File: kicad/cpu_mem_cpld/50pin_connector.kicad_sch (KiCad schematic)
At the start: 1 part, among them P5 CONN_02X25

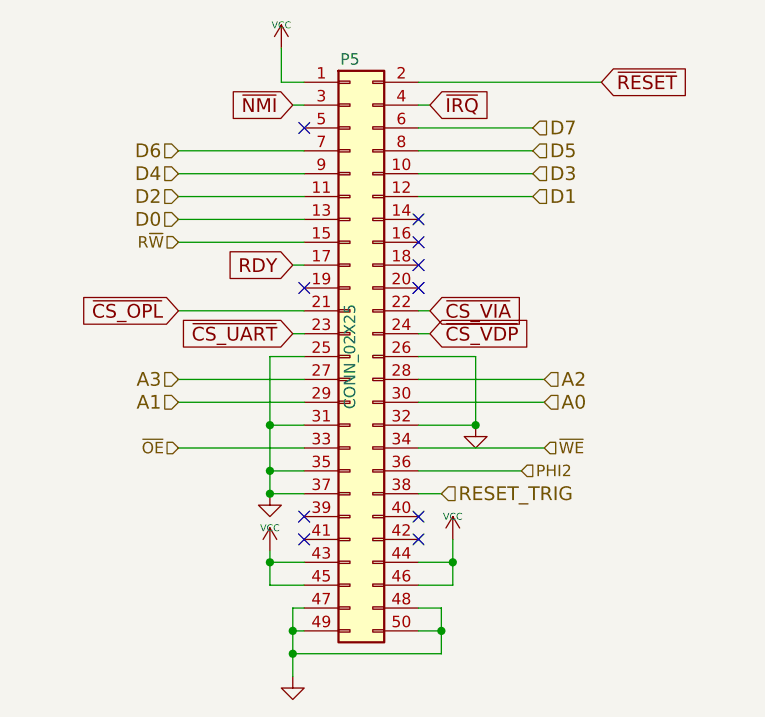
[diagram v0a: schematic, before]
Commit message: remove all global labels
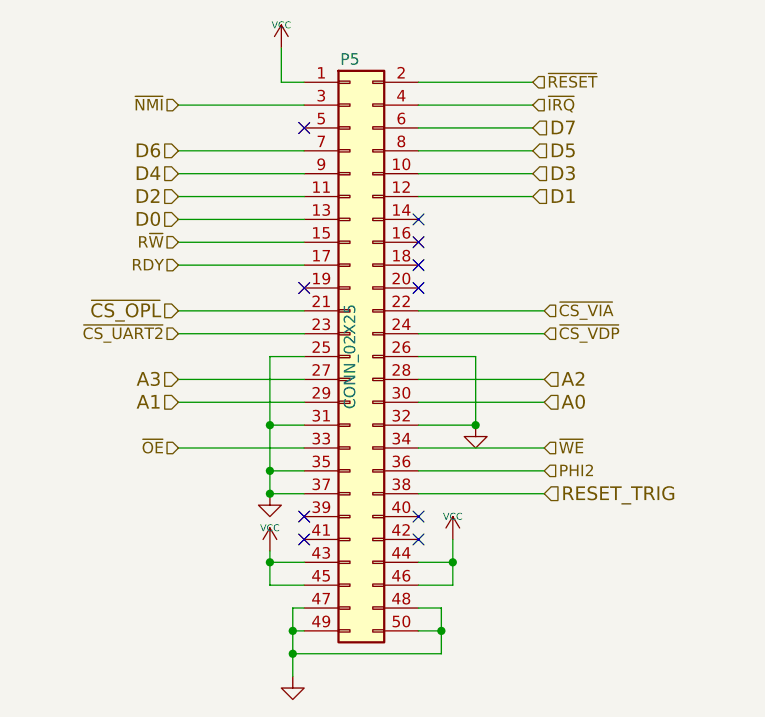
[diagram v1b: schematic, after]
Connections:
- net ~{CS_UART} renamed ~{CS_UART2}
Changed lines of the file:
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@@
     (stroke (width 0) (type default) (color 0 0 0 0))
   )
-  (wire (pts (xy 147.32 92.71) (xy 148.59 92.71))
+  (wire (pts (xy 147.32 92.71) (xy 161.29 92.71))
     (stroke (width 0) (type default) (color 0 0 0 0))
   )
@@
     (stroke (width 0) (type default) (color 0 0 0 0))
   )
-  (wire (pts (xy 147.32 64.77) (xy 167.64 64.77))
+  (wire (pts (xy 147.32 64.77) (xy 160.02 64.77))
     (stroke (width 0) (type default) (color 0 0 0 0))
   )
@@
     (stroke (width 0) (type default) (color 0 0 0 0))
   )
-  (wire (pts (xy 134.62 67.31) (xy 133.35 67.31))
+  (wire (pts (xy 134.62 67.31) (xy 120.65 67.31))
     (stroke (width 0) (type default) (color 0 0 0 0))
   )
@@
     (stroke (width 0) (type default) (color 0 0 0 0))
   )
-  (wire (pts (xy 147.32 90.17) (xy 148.59 90.17))
+  (wire (pts (xy 147.32 90.17) (xy 161.29 90.17))
     (stroke (width 0) (type default) (color 0 0 0 0))
   )
@@
     (stroke (width 0) (type default) (color 0 0 0 0))
   )
-  (wire (pts (xy 147.32 110.49) (xy 149.86 110.49))
+  (wire (pts (xy 147.32 110.49) (xy 161.29 110.49))
     (stroke (width 0) (type default) (color 0 0 0 0))
   )
@@
     (stroke (width 0) (type default) (color 0 0 0 0))
   )
-  (wire (pts (xy 147.32 67.31) (xy 148.59 67.31))
+  (wire (pts (xy 147.32 67.31) (xy 160.02 67.31))
     (stroke (width 0) (type default) (color 0 0 0 0))
   )
@@
     (stroke (width 0) (type default) (color 0 0 0 0))
   )
-  (wire (pts (xy 147.32 107.95) (xy 158.75 107.95))
+  (wire (pts (xy 147.32 107.95) (xy 161.29 107.95))
     (stroke (width 0) (type default) (color 0 0 0 0))
   )
@@
     (stroke (width 0) (type default) (color 0 0 0 0))
   )
-  (wire (pts (xy 133.35 85.09) (xy 134.62 85.09))
+  (wire (pts (xy 120.65 85.09) (xy 134.62 85.09))
     (stroke (width 0) (type default) (color 0 0 0 0))
   )
@@
     (stroke (width 0) (type default) (color 0 0 0 0))
   )
-  (wire (pts (xy 134.62 92.71) (xy 133.35 92.71))
+  (wire (pts (xy 120.65 92.71) (xy 134.62 92.71))
     (stroke (width 0) (type default) (color 0 0 0 0))
   )
@@
     (stroke (width 0) (type default) (color 0 0 0 0))
   )
-  (global_label "~{CS_VDP}" (shape input) (at 148.59 92.71 0) (fields_autoplaced)
-    (effects (font (size 1.524 1.524)) (justify left))
-    (property "Intersheet References" "${INTERSHEET_REFS}" (id 0) (at 0 0 0)
-      (effects (font (size 1.27 1.27)) hide)
-    )
-  )
-  (global_label "~{IRQ}" (shape input) (at 148.59 67.31 0) (fields_autoplaced)
-    (effects (font (size 1.524 1.524)) (justify left))
-    (property "Intersheet References" "${INTERSHEET_REFS}" (id 0) (at 0 0 0)
-      (effects (font (size 1.27 1.27)) hide)
-    )
-  )
-  (global_label "~{RESET}" (shape input) (at 167.64 64.77 0) (fields_autoplaced)
-    (effects (font (size 1.524 1.524)) (justify left))
-    (property "Intersheet References" "${INTERSHEET_REFS}" (id 0) (at 0 0 0)
-      (effects (font (size 1.27 1.27)) hide)
-    )
-  )
-  (global_label "~{NMI}" (shape input) (at 133.35 67.31 180) (fields_autoplaced)
-    (effects (font (size 1.524 1.524)) (justify right))
-    (property "Intersheet References" "${INTERSHEET_REFS}" (id 0) (at 0 0 0)
-      (effects (font (size 1.27 1.27)) hide)
-    )
-  )
-  (global_label "~{CS_UART}" (shape input) (at 133.35 92.71 180) (fields_autoplaced)
-    (effects (font (size 1.524 1.524)) (justify right))
-    (property "Intersheet References" "${INTERSHEET_REFS}" (id 0) (at 0 0 0)
-      (effects (font (size 1.27 1.27)) hide)
-    )
-  )
-  (global_label "RDY" (shape input) (at 133.35 85.09 180) (fields_autoplaced)
-    (effects (font (size 1.524 1.524)) (justify right))
-    (property "Intersheet References" "${INTERSHEET_REFS}" (id 0) (at 0 0 0)
-      (effects (font (size 1.27 1.27)) hide)
-    )
-  )
-  (global_label "~{CS_VIA}" (shape input) (at 148.59 90.17 0) (fields_autoplaced)
-    (effects (font (size 1.524 1.524)) (justify left))
-    (property "Intersheet References" "${INTERSHEET_REFS}" (id 0) (at 0 0 0)
-      (effects (font (size 1.27 1.27)) hide)
-    )
-  )
-  (global_label "~{CS_OPL}" (shape input) (at 120.65 90.17 180) (fields_autoplaced)
-    (effects (font (size 1.524 1.524)) (justify right))
-    (property "Intersheet References" "${INTERSHEET_REFS}" (id 0) (at 0 0 0)
-      (effects (font (size 1.27 1.27)) hide)
-    )
-  )
   (hierarchical_label "D1" (shape input) (at 160.02 77.47 0)
     (effects (font (size 1.524 1.524)) (justify left))
@@
     (effects (font (size 1.524 1.524)) (justify left))
   )
+  (hierarchical_label "~{CS_OPL}" (shape input) (at 120.65 90.17 180)
+    (effects (font (size 1.524 1.524)) (justify right))
+  )
   (hierarchical_label "~{WE}" (shape input) (at 161.29 105.41 0)
     (effects (font (size 1.27 1.27)) (justify left))
@@
     (effects (font (size 1.524 1.524)) (justify right))
   )
-  (hierarchical_label "PHI2" (shape input) (at 158.75 107.95 0)
+  (hierarchical_label "PHI2" (shape input) (at 161.29 107.95 0)
     (effects (font (size 1.27 1.27)) (justify left))
   )
@@
     (effects (font (size 1.27 1.27)) (justify right))
   )
+  (hierarchical_label "~{CS_VDP}" (shape input) (at 161.29 92.71 0)
+    (effects (font (size 1.27 1.27)) (justify left))
+  )
   (hierarchical_label "A3" (shape input) (at 120.65 97.79 180)
     (effects (font (size 1.524 1.524)) (justify right))
@@
     (effects (font (size 1.524 1.524)) (justify right))
   )
+  (hierarchical_label "~{NMI}" (shape input) (at 120.65 67.31 180)
+    (effects (font (size 1.27 1.27)) (justify right))
+  )
   (hierarchical_label "D3" (shape input) (at 160.02 74.93 0)
     (effects (font (size 1.524 1.524)) (justify left))
   )
-  (hierarchical_label "RESET_TRIG" (shape input) (at 149.86 110.49 0)
+  (hierarchical_label "~{CS_VIA}" (shape input) (at 161.29 90.17 0)
+    (effects (font (size 1.27 1.27)) (justify left))
+  )
+  (hierarchical_label "RESET_TRIG" (shape input) (at 161.29 110.49 0)
     (effects (font (size 1.524 1.524)) (justify left))
   )
@@
     (effects (font (size 1.524 1.524)) (justify right))
   )
+  (hierarchical_label "~{RESET}" (shape input) (at 160.02 64.77 0)
+    (effects (font (size 1.27 1.27)) (justify left))
+  )
+  (hierarchical_label "RDY" (shape input) (at 120.65 85.09 180)
+    (effects (font (size 1.27 1.27)) (justify right))
+  )
+  (hierarchical_label "~{CS_UART2}" (shape input) (at 120.65 92.71 180)
+    (effects (font (size 1.27 1.27)) (justify right))
+  )
   (hierarchical_label "D6" (shape input) (at 120.65 72.39 180)
     (effects (font (size 1.524 1.524)) (justify right))
   )
+  (hierarchical_label "~{IRQ}" (shape input) (at 160.02 67.31 0)
+    (effects (font (size 1.27 1.27)) (justify left))
+  )
   (symbol (lib_id "Connector_Generic:Conn_02x25_Odd_Even") (at 139.7 95.25 0) (unit 1)
